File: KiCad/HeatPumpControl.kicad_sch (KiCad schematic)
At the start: 44 parts, among them J1 Conn_01x04_Male, J2 Conn_01x04_Male, J3 Conn_01x04_Male, J4 Conn_01x03_Male, Q1 2N2222A, Q2 Q_PMOS_GDS, U1 TSOP23xx, U3 XIAO-ESP32-C6-SMD

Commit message: Add GPIO descriptions and other texts
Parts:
- added D8: 1N4148, Diode_SMD:D_SOD-323, symbol Diode:1N4148
- D10, D7, R10, R20, R22: now not fitted
- R15: value 51.2k -> 68k
- R17: value 82k -> 1M
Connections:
- net ON: now also D8.1 (K)
- net at C2.1, J4.2 (Pin_2), Q2.1 (G)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: now also D8.2 (A)
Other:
- note added: "ESP32C3: GPIO2/D0 - PULLED UP - N/A GPIO3/A1 - General IO, no pull-up GPIO4/D2 - IR out GPIO5/D3 - PIR, 1-Wire, open drain/collector, GPIO6/D4 - I2C SDA GPIO7/D5 - I2C SCL GPIO8/D8 - PULLED UP - N/A GPIO9/D9 - ILED GPIO10D10 - PIR, 1-Wire, open drain/collector, GPIO21/D6 - RX <--> TX GPIO20/D7 - TX <--> RX Avoid GPIO 0,8,9 ESP32C6: GPIO0/D0 - /BAT READ GPIO1/A1 - BAT Vin GPIO2/D2 - IR out GPIO21/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"
- note added: "NOTES: LED D1+D2+(and D3) should not be present if +VBAT is from LiPo D7, D10 normally not used - when R18 R16 is used R20 and R22 normally not used R19 only used with LiPo battery"
- note removed: "D0 - PULLED UP - N/A A1 - General IO, no pull-uo D2 - IR out D3 - PIR, 1-Wire, open drain/collector, any pulled up D4 - I2C SDA D5 - I2C SCL D8 - PULLED UP - N/A D9 - ILED D10 - PIR, 1-Wire, open drain/collector, any pulled up D6 - RX <--> TX D7 - TX <--> RX"
- note removed: "NOTES: D7, D9, D10 normally 0 ohm R10 and R12 normally unused ERRORS: H2 / IR receiver has no GND Q1 is upside down"
- title: Heat pump ctrl / generic IO  -> ESP32C3/C6 with serial port, IR sender, I2C and battery operation
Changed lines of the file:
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@@
 	(paper "A4")
 	(title_block
-		(title "Heat pump ctrl / generic IO ")
-		(date "2025-10-28")
-		(rev "v4.0")
+		(title "ESP32C3/C6 with serial port, IR sender, I2C and battery operation")
+		(date "2025-12-01")
+		(rev "v4.0.1")
 		(company "Hans Rune Bue <email@hansrune.net>")
 		(comment 1 "Hardware is licensed under CERN-OHL-W-2.0")
 		(comment 2 "Project documents are licensed under CC-BY-SA 2.0")
+		(comment 3 "PCB version 4.0.0 can still be used")
 	)
 	(text "Strapping pins:\n\nIO8  IO9 \n NA   1   SPI boot (default) Flash boot\n 1    0   Download"
 		(exclude_from_sim no)
-		(at 19.05 193.04 0)
+		(at 17.526 177.038 0)
 		(effects
 			(font
-				(size 2.54 2.54)
+				(size 2 2)
 			)
 			(justify left bottom)
 		)
 	)
-	(text "NOTES:\n  D7, D9, D10 normally 0 ohm\n  R10 and R12 normally unused\n\nERRORS:\n  H2 / IR receiver has no GND\n  Q1 is upside down \n   "
+	(text "NOTES:\n  LED D1+D2+(and D3) should not be present if +VBAT is from LiPo\n  D7, D10 normally not used - when R18 R16 is used\n  R20 and R22 normally not used\n  R19 only used with LiPo battery\n\n   "
 		(exclude_from_sim no)
-		(at 212.09 124.46 0)
+		(at 16.002 201.676 0)
 		(effects
 			(font
-				(size 2.54 2.54)
+				(size 2 2)
 			)
 			(justify left bottom)
 		)
 	)
-	(text "D0  - PULLED UP - N/A\nA1  - General IO, no pull-uo\nD2  - IR out\nD3  - PIR, 1-Wire,\n           open drain/collector,\n           any pulled up\nD4  - I2C SDA\nD5  - I2C SCL\nD8  - PULLED UP - N/A\nD9  - ILED\nD10 - PIR, 1-Wire, \n           open drain/collector,\n           any pulled up\nD6  - RX <--> TX\nD7  - TX <--> RX"
+	(text "ESP32C3:\n  GPIO2/D0  - PULLED UP - N/A\n  GPIO3/A1  - General IO, no pull-up\n  GPIO4/D2  - IR out\n  GPIO5/D3  - PIR, 1-Wire,\n              open drain/collector,\n  GPIO6/D4  - I2C SDA\n  GPIO7/D5  - I2C SCL\n  GPIO8/D8  - PULLED UP - N/A\n  GPIO9/D9  - ILED\n  GPIO10D10 - PIR, 1-Wire, \n              open drain/collector,\n  GPIO21/D6  - RX <--> TX\n  GPIO20/D7  - TX <--> RX\n\n  Avoid GPIO 0,8,9\n\n\nESP32C6:\n\n  GPIO0/D0   - /BAT READ\n  GPIO1/A1   - BAT Vin\n  GPIO2/D2   - IR out\n  GPIO21/D3  - PIR, 1-Wire,\n               open drain/collector,\n               any pulled up\n  GPIO22/D4  - I2C SDA\n  GPIO23/D5  - I2C SCL\n  GPIO20/D9  - ILED\n  GPIO18/D10 - PIR, 1-Wire,\n               open drain/collector,\n               any pulled up\n  GPIO17/D7  - RX / 1-wire\n  GPIO16/D6  - TX / 1-wire\n\n  GPIO3      - /Antenna chip\n  GPIO14     - H=ext antenna\n  GPIO15     - /Module yellow LED\n\n  Avoid GPIO 4,5,8,9,15\n"
 		(exclude_from_sim no)
-		(at 212.09 85.09 0)
+		(at 222.504 146.558 0)
 		(effects
 			(font
-				(size 2.54 2.54)
+				(size 2 2)
 			)
 			(justify left bottom)
@@
 	)
 	(junction
+		(at 33.02 88.9)
+		(diameter 0)
+		(color 0 0 0 0)
+	)
+	(junction
 		(at 170.18 143.51)
 		(diameter 0)
@@
 	)
 	(junction
+		(at 33.02 78.74)
+		(diameter 0)
+		(color 0 0 0 0)
+	)
+	(junction
 		(at 38.1 121.92)
 		(diameter 0)
@@
 	(wire
 		(pts
+			(xy 33.02 78.74) (xy 33.02 80.01)
+		)
+		(stroke
+			(width 0)
+			(type default)
+		)
+	)
+	(wire
+		(pts
 			(xy 54.61 50.8) (xy 54.61 58.42)
 		)
@@
 	(wire
 		(pts
+			(xy 27.94 88.9) (xy 33.02 88.9)
+		)
+		(stroke
+			(width 0)
+			(type default)
+		)
+	)
+	(wire
+		(pts
 			(xy 151.13 67.31) (xy 151.13 64.77)
 		)
@@
 	(wire
 		(pts
-			(xy 33.02 53.34) (xy 33.02 80.01)
+			(xy 33.02 53.34) (xy 33.02 78.74)
 		)
 		(stroke
@@
 	(wire
 		(pts
+			(xy 33.02 88.9) (xy 33.02 110.49)
+		)
+		(stroke
+			(width 0)
+			(type default)
+		)
+	)
+	(wire
+		(pts
 			(xy 40.64 52.07) (xy 40.64 53.34)
 		)
@@
 	(wire
 		(pts
+			(xy 27.94 78.74) (xy 33.02 78.74)
+		)
+		(stroke
+			(width 0)
+			(type default)
+		)
+	)
+	(wire
+		(pts
 			(xy 163.83 90.17) (xy 163.83 91.44)
 		)
@@
 	(wire
 		(pts
+			(xy 27.94 87.63) (xy 27.94 88.9)
+		)
+		(stroke
+			(width 0)
+			(type default)
+		)
+	)
+	(wire
+		(pts
 			(xy 21.59 113.03) (xy 21.59 114.3)
 		)
@@
 	(wire
 		(pts
+			(xy 27.94 80.01) (xy 27.94 78.74)
+		)
+		(stroke
+			(width 0)
+			(type default)
+		)
+	)
+	(wire
+		(pts
 			(xy 49.53 133.35) (xy 49.53 134.62)
 		)
@@
 	(wire
 		(pts
-			(xy 33.02 87.63) (xy 33.02 110.49)
+			(xy 33.02 87.63) (xy 33.02 88.9)
 		)
 		(stroke
@@
 		)
 		(property "Value" "1N4148"
-			(at 181.61 102.87 0)
+			(at 180.594 97.536 0)
 			(effects
 				(font
@@
 				)
 				(justify right)
-				(hide yes)
 			)
 		)
@@
 		(in_bom yes)
 		(on_board yes)
-		(dnp no)
+		(dnp yes)
 		(property "Reference" "D10"
 			(at 176.53 153.67 0)
@@
 		(in_bom yes)
 		(on_board yes)
-		(dnp no)
+		(dnp yes)
 		(property "Reference" "D7"
 			(at 171.45 148.59 0)
@@
 		(in_bom yes)
 		(on_board yes)
-		(dnp no)
+		(dnp yes)
 		(property "Reference" "R10"
 			(at 190.5 135.382 90)
@@
 		(in_bom yes)
 		(on_board yes)
-		(dnp no)
+		(dnp yes)
 		(property "Reference" "R20"
-			(at 29.972 84.074 0)
+			(at 35.306 84.074 90)
 			(effects
 				(font
@@
 			)
 		)
-		(property "Value" "51.2k"
+		(property "Value" "68k"
 			(at 50.546 64.516 90)
 			(effects
@@
 			)
 		)
-		(property "Value" "82k"
+		(property "Value" "1M"
 			(at 43.18 49.53 90)
 			(effects
@@
 		(dnp no)
 		(property "Reference" "R19"
-			(at 106.934 107.188 90)
+			(at 106.68 102.616 90)
 			(effects
 				(font
@@
 		(in_bom yes)
 		(on_board yes)
-		(dnp no)
+		(dnp yes)
 		(property "Reference" "R22"
-			(at 177.292 101.6 90)
+			(at 177.546 106.426 90)
 			(effects
 				(font
@@
 					(unit 1)
 				)
+			)
+		)
+	)
+	(symbol
+		(lib_id "Diode:1N4148")
+		(at 27.94 83.82 90)
+		(unit 1)
+		(exclude_from_sim no)
+		(in_bom yes)
+		(on_board yes)
+		(dnp no)
+		(property "Reference" "D8"
+			(at 25.146 82.804 0)
+			(effects
+				(font
+					(size 1.27 1.27)
+				)
+				(justify right)
+			)
+		)
+		(property "Value" "1N4148"
+			(at 29.9466 84.963 90)
+			(effects
+				(font
+					(size 1.27 1.27)
+				)
+				(justify right)
+				(hide yes)
+			)
+		)
+		(property "Footprint" "Diode_SMD:D_SOD-323"
+			(at 32.385 83.82 0)
+			(effects
+				(font
+					(size 1.27 1.27)
+				)
+				(hide yes)
+			)
+		)
+		(property "Datasheet" "http://www.nxp.com/documents/data_sheet/1N4148_1N4448.pdf"
+			(at 27.94 83.82 0)
+			(effects
+				(font
+					(size 1.27 1.27)
+				)
+				(hide yes)
+			)
+		)
+		(property "Description" ""
+			(at 27.94 83.82 0)
+			(effects
+				(font
+					(size 1.27 1.27)
+				)
+				(hide yes)
+			)
+		)
+		(pin "1"
+		)
+		(pin "2"
+		)
+		(instances
+			(project "HeatPumpControl"
+				(path "/2a5b3e3c-2022-46db-8938-2c3b2e9edb6d"
+					(reference "D8")
+					(unit 1)
+				)

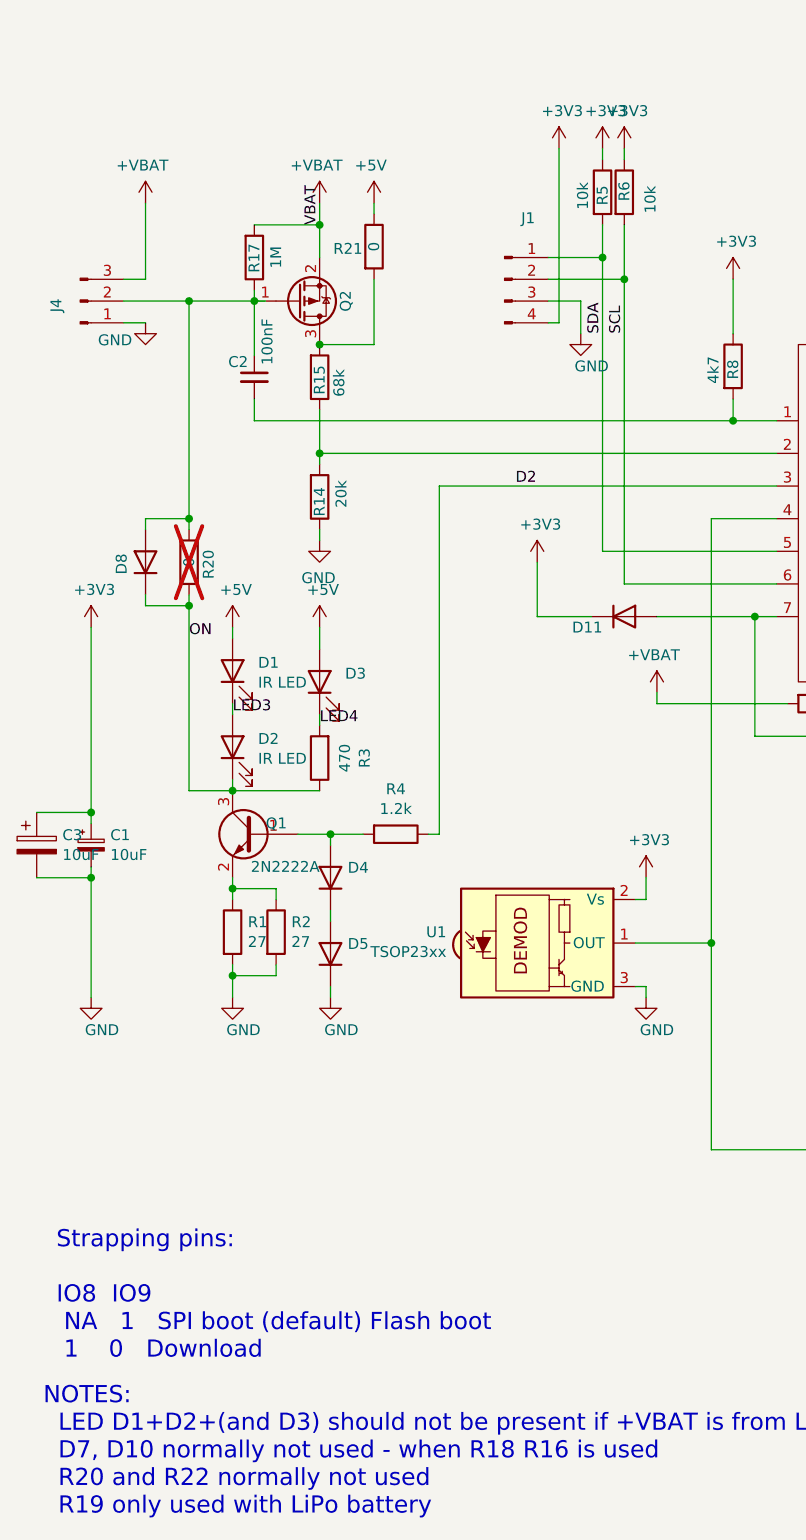
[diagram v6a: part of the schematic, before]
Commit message: Add diode for VBAT -> 5V
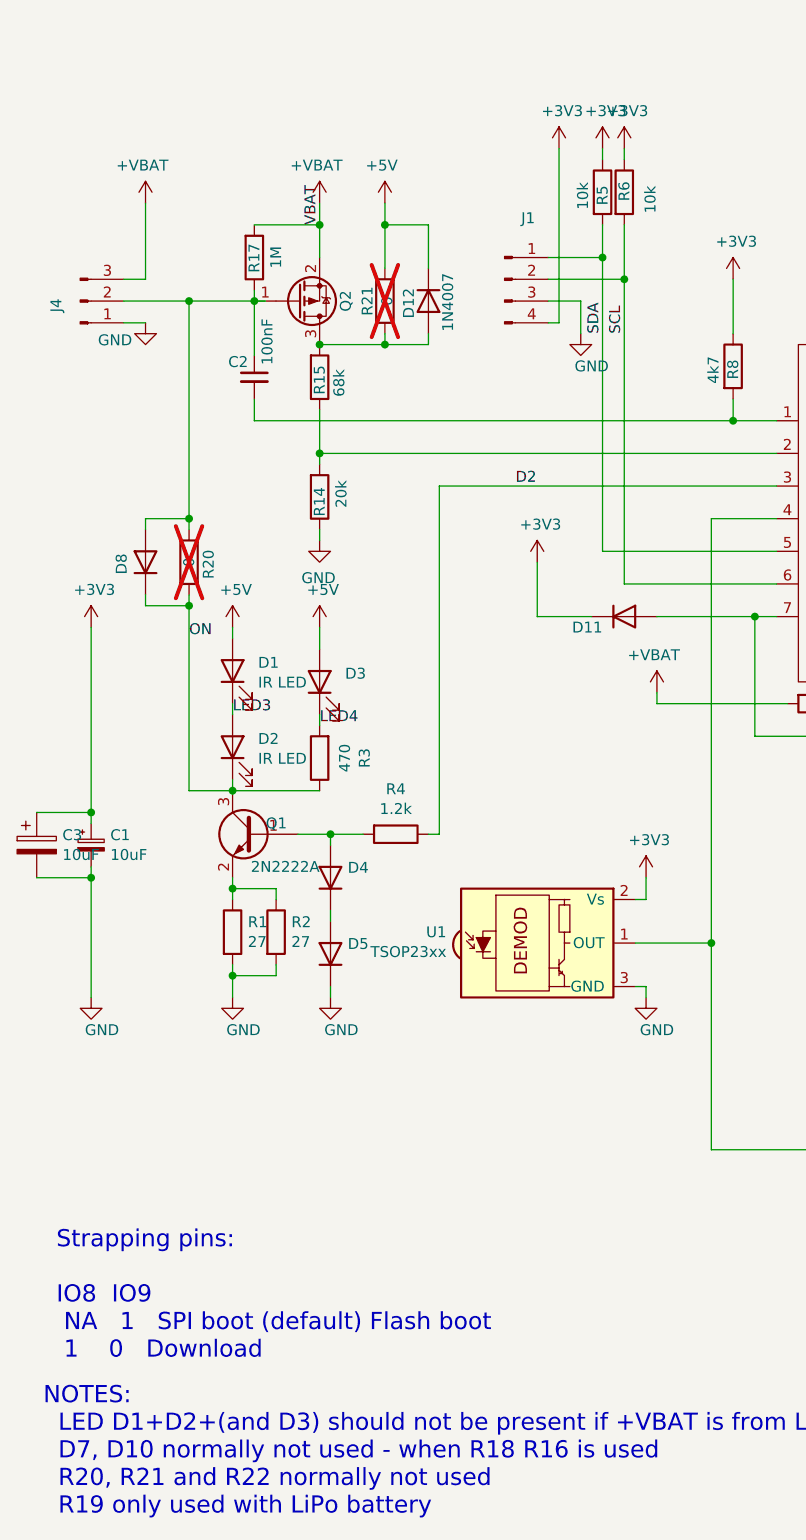
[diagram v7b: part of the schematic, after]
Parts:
- added D12: 1N4007, Diode_SMD:D_SOD-323, symbol Diode:1N4148
- R21: now not fitted
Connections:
- net +5V: now also D12.1 (K)
- net at Q2.3 (D), R15.2, R21.2: now also D12.2 (A)
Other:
- note added: "NOTES: LED D1+D2+(and D3) should not be present if +VBAT is from LiPo D7, D10 normally not used - when R18 R16 is used R20, R21 and R22 normally not used R19 only used with LiPo battery"
- note removed: "NOTES: LED D1+D2+(and D3) should not be present if +VBAT is from LiPo D7, D10 normally not used - when R18 R16 is used R20 and R22 normally not used R19 only used with LiPo battery"
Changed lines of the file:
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@@
 	(title_block
 		(title "ESP32C3/C6 with serial port, IR sender, I2C and battery operation")
-		(date "2025-12-01")
-		(rev "v4.0.1")
+		(date "2025-12-04")
+		(rev "v4.0.2")
 		(company "Hans Rune Bue <email@hansrune.net>")
 		(comment 1 "Hardware is licensed under CERN-OHL-W-2.0")
@@
 		)
 	)
-	(text "NOTES:\n  LED D1+D2+(and D3) should not be present if +VBAT is from LiPo\n  D7, D10 normally not used - when R18 R16 is used\n  R20 and R22 normally not used\n  R19 only used with LiPo battery\n\n   "
+	(text "NOTES:\n  LED D1+D2+(and D3) should not be present if +VBAT is from LiPo\n  D7, D10 normally not used - when R18 R16 is used\n  R20, R21 and R22 normally not used\n  R19 only used with LiPo battery\n\n   "
 		(exclude_from_sim no)
 		(at 16.002 201.676 0)
@@
 	)
 	(junction
+		(at 55.88 44.45)
+		(diameter 0)
+		(color 0 0 0 0)
+	)
+	(junction
+		(at 55.88 58.42)
+		(diameter 0)
+		(color 0 0 0 0)
+	)
+	(junction
 		(at 171.45 104.14)
 		(diameter 0)
@@
 	(wire
 		(pts
+			(xy 60.96 44.45) (xy 55.88 44.45)
+		)
+		(stroke
+			(width 0)
+			(type default)
+		)
+	)
+	(wire
+		(pts
 			(xy 21.59 119.38) (xy 21.59 120.65)
 		)
@@
 	(wire
 		(pts
-			(xy 54.61 50.8) (xy 54.61 58.42)
+			(xy 55.88 57.15) (xy 55.88 58.42)
 		)
 		(stroke
@@
 	(wire
 		(pts
+			(xy 55.88 58.42) (xy 60.96 58.42)
+		)
+		(stroke
+			(width 0)
+			(type default)
+		)
+	)
+	(wire
+		(pts
 			(xy 96.52 67.31) (xy 101.6 67.31)
 		)
@@
 	(wire
 		(pts
+			(xy 55.88 44.45) (xy 55.88 49.53)
+		)
+		(stroke
+			(width 0)
+			(type default)
+		)
+	)
+	(wire
+		(pts
 			(xy 144.78 71.12) (xy 146.05 71.12)
 		)
@@
 	(wire
 		(pts
+			(xy 60.96 58.42) (xy 60.96 57.15)
+		)
+		(stroke
+			(width 0)
+			(type default)
+		)
+	)
+	(wire
+		(pts
 			(xy 182.88 152.4) (xy 185.42 152.4)
 		)
@@
 	(wire
 		(pts
+			(xy 60.96 49.53) (xy 60.96 44.45)
+		)
+		(stroke
+			(width 0)
+			(type default)
+		)
+	)
+	(wire
+		(pts
 			(xy 15.24 113.03) (xy 21.59 113.03)
 		)
@@
 	(wire
 		(pts
-			(xy 54.61 41.91) (xy 54.61 43.18)
+			(xy 55.88 41.91) (xy 55.88 44.45)
 		)
 		(stroke
@@
 	(wire
 		(pts
-			(xy 48.26 58.42) (xy 54.61 58.42)
+			(xy 48.26 58.42) (xy 55.88 58.42)
 		)
 		(stroke
@@
 	(symbol
 		(lib_id "Device:R")
-		(at 54.61 46.99 0)
+		(at 55.88 53.34 0)
 		(unit 1)
 		(exclude_from_sim no)
 		(in_bom yes)
 		(on_board yes)
-		(dnp no)
+		(dnp yes)
 		(property "Reference" "R21"
-			(at 51.562 47.244 0)
+			(at 53.848 53.34 90)
 			(effects
 				(font
@@
 		)
 		(property "Value" "0"
-			(at 54.61 46.99 90)
+			(at 56.134 53.34 90)
 			(effects
 				(font
@@
 		)
 		(property "Footprint" "Resistor_SMD:R_0805_2012Metric"
-			(at 52.832 46.99 90)
+			(at 54.102 53.34 90)
 			(effects
 				(font
@@
 		)
 		(property "Datasheet" "~"
-			(at 54.61 46.99 0)
+			(at 55.88 53.34 0)
 			(effects
 				(font
@@
 		)
 		(property "Description" ""
-			(at 54.61 46.99 0)
+			(at 55.88 53.34 0)
 			(effects
 				(font
@@
 	(symbol
 		(lib_id "power:+5V")
-		(at 54.61 41.91 0)
+		(at 55.88 41.91 0)
 		(mirror y)
 		(unit 1)
@@
 		(dnp no)
 		(property "Reference" "#PWR034"
-			(at 54.61 45.72 0)
+			(at 55.88 45.72 0)
 			(effects
 				(font
@@
 		)
 		(property "Value" "+5V"
-			(at 54.229 37.5158 0)
+			(at 55.499 37.5158 0)
 			(effects
 				(font
@@
 		)
 		(property "Footprint" ""
-			(at 54.61 41.91 0)
+			(at 55.88 41.91 0)
 			(effects
 				(font
@@
 		)
 		(property "Datasheet" ""
-			(at 54.61 41.91 0)
+			(at 55.88 41.91 0)
 			(effects
 				(font
@@
 		)
 		(property "Description" ""
-			(at 54.61 41.91 0)
+			(at 55.88 41.91 0)
 			(effects
 				(font
@@
 					(unit 1)
 				)
+			)
+		)
+	)
+	(symbol
+		(lib_id "Diode:1N4148")
+		(at 60.96 53.34 270)
+		(unit 1)
+		(exclude_from_sim no)
+		(in_bom yes)
+		(on_board yes)
+		(dnp no)
+		(property "Reference" "D12"
+			(at 58.674 55.372 0)
+			(effects
+				(font
+					(size 1.27 1.27)
+				)
+				(justify right)
+			)
+		)
+		(property "Value" "1N4007"
+			(at 63.246 56.896 0)
+			(effects
+				(font
+					(size 1.27 1.27)
+				)
+				(justify right)
+			)
+		)
+		(property "Footprint" "Diode_SMD:D_SOD-323"
+			(at 56.515 53.34 0)
+			(effects
+				(font
+					(size 1.27 1.27)
+				)
+				(hide yes)
+			)
+		)
+		(property "Datasheet" ""
+			(at 60.96 53.34 0)
+			(effects
+				(font
+					(size 1.27 1.27)
+				)
+				(hide yes)
+			)
+		)
+		(property "Description" ""
+			(at 60.96 53.34 0)
+			(effects
+				(font
+					(size 1.27 1.27)
+				)
+				(hide yes)
+			)
+		)
+		(pin "1"
+		)
+		(pin "2"
+		)
+		(instances
+			(project "HeatPumpControl"
+				(path "/2a5b3e3c-2022-46db-8938-2c3b2e9edb6d"
+					(reference "D12")
+					(unit 1)
+				)

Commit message: Change to SOD-123 for 1N4007
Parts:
- D12: footprint Diode_SMD:D_SOD-323 -> Diode_SMD:D_SOD-123
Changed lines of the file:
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@@
 	(title_block
 		(title "ESP32C3/C6 with serial port, IR sender, I2C and battery operation")
-		(date "2025-12-04")
-		(rev "v4.0.2")
+		(date "2025-12-23")
+		(rev "v4.0.3")
 		(company "Hans Rune Bue <email@hansrune.net>")
 		(comment 1 "Hardware is licensed under CERN-OHL-W-2.0")
@@
 			)
 		)
-		(property "Footprint" "Diode_SMD:D_SOD-323"
+		(property "Footprint" "Diode_SMD:D_SOD-123"
 			(at 56.515 53.34 0)
 			(effects
